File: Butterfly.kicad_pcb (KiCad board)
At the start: 2 copper layers, 93.1 x 65.5 mm, 0 parts

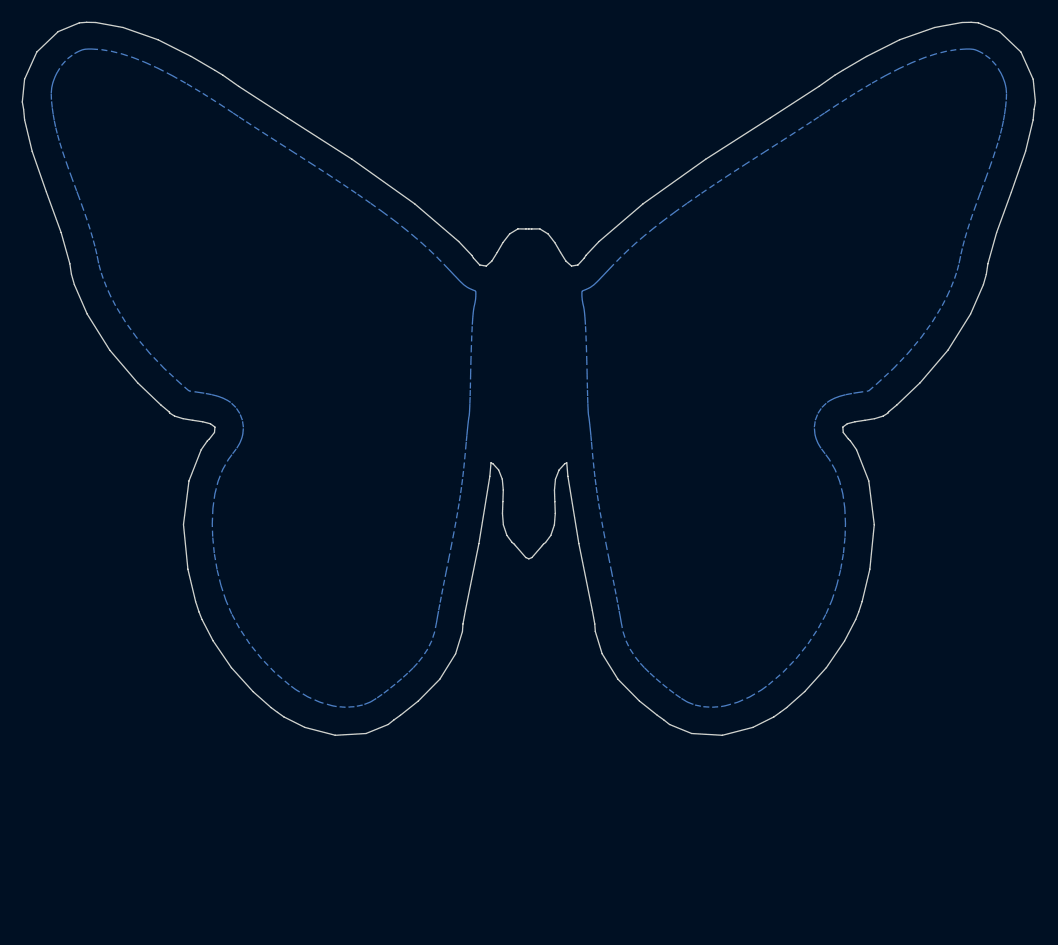
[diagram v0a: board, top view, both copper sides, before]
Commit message: Change copper layer to F.Cu.
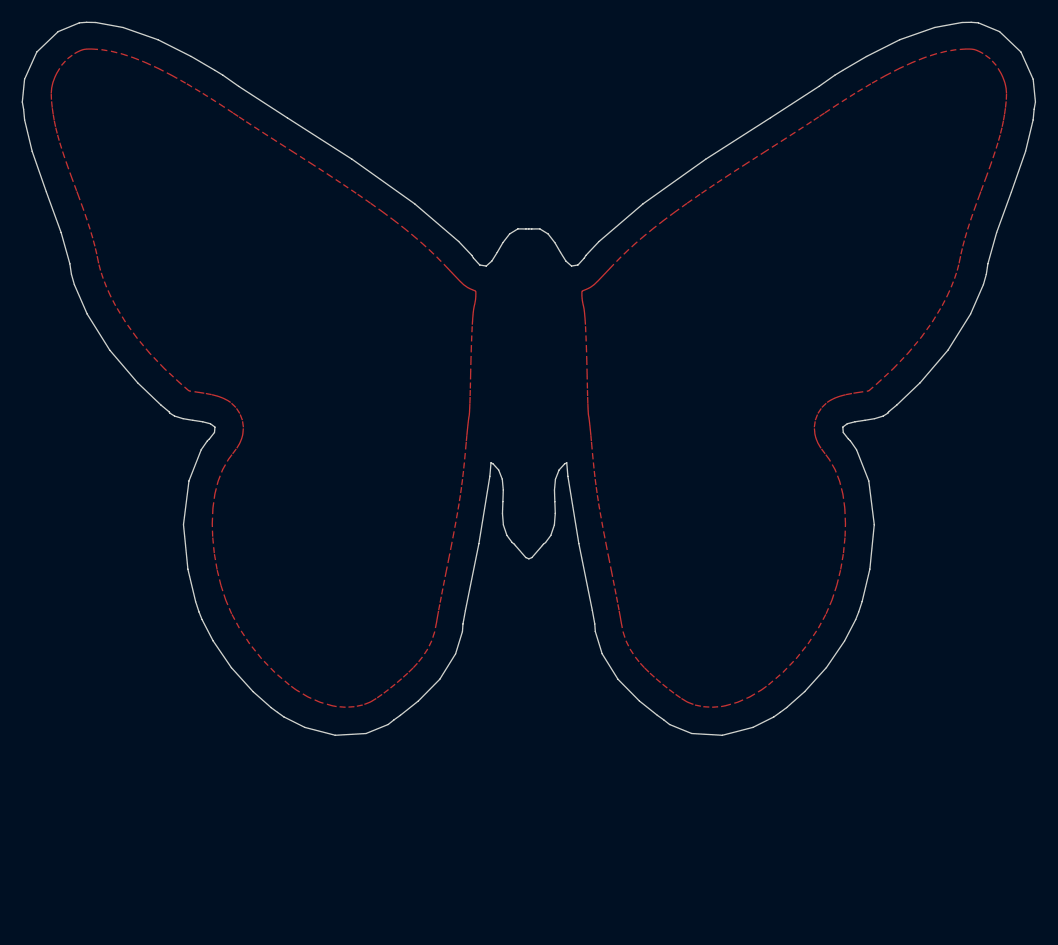
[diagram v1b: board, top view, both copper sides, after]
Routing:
- added copper zone on F.Cu, net (none)
- removed copper zone on B.Cu, net (none)
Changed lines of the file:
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@@
   (gr_line (start 161.23777 81.9574) (end 167.20467 78.1404) (layer Edge.Cuts) (width 0.1))
   (gr_line (start 183.5 99.5) (end 180.94377 102.4917) (layer Edge.Cuts) (width 0.1))
-  (zone (net 0) (net_name "") (layer B.Cu) (hatch edge 0.508)
+  (zone (net 0) (net_name "") (layer F.Cu) (hatch edge 0.508)
     (connect_pads (clearance 0.508))
     (min_thickness 0.254)
@@
     )
   )
-  (zone (net 0) (net_name "") (layer B.Cu) (hatch edge 0.508)
+  (zone (net 0) (net_name "") (layer F.Cu) (hatch edge 0.508)
     (connect_pads (clearance 0.508))
     (min_thickness 0.254)

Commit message: Instantiate left wing markings.
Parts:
- added G***: LOGO, myLibrary:copper-on-wing-left, F.Cu at (121.5, 101.5)

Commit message: Copper patterns on both wings.
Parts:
- added G***: LOGO, myLibrary:copper-on-wing-right, F.Cu at (168.5, 101.5)

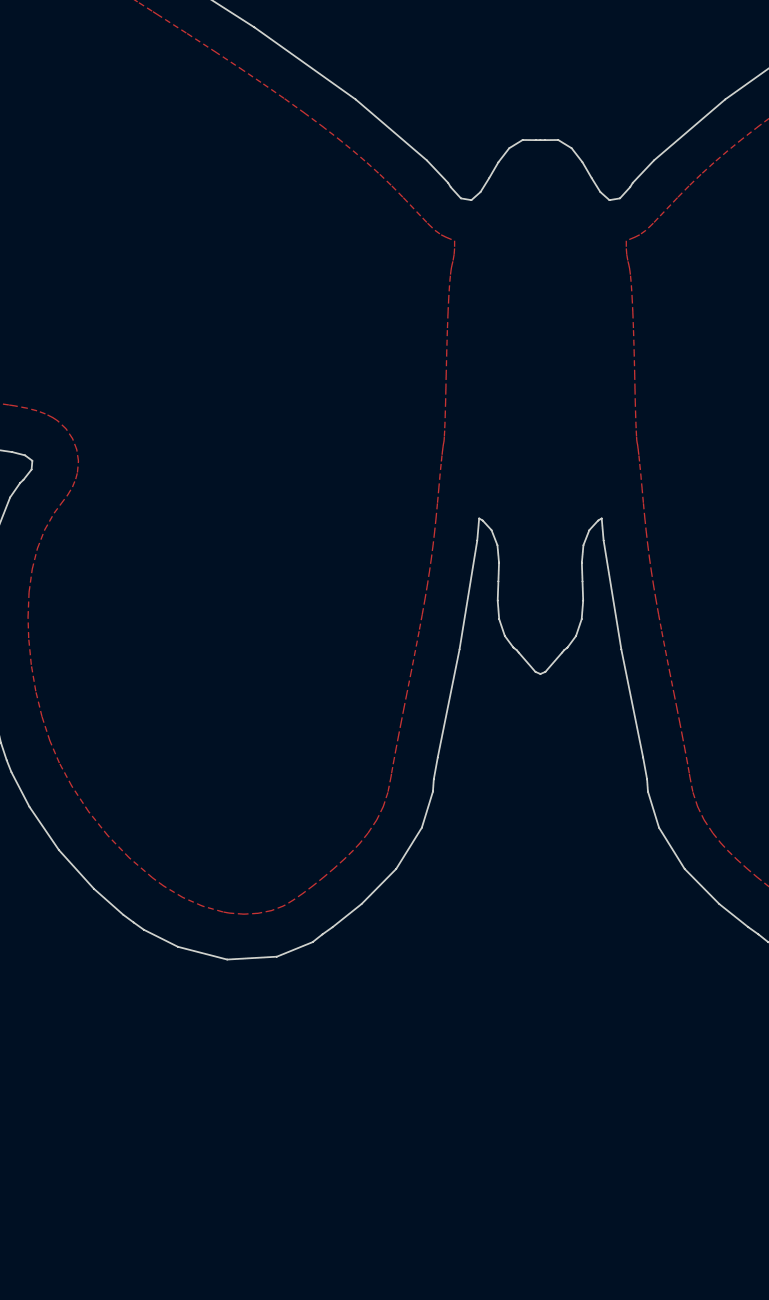
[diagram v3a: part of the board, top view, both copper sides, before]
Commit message: Trying to position footprints; not enough room.
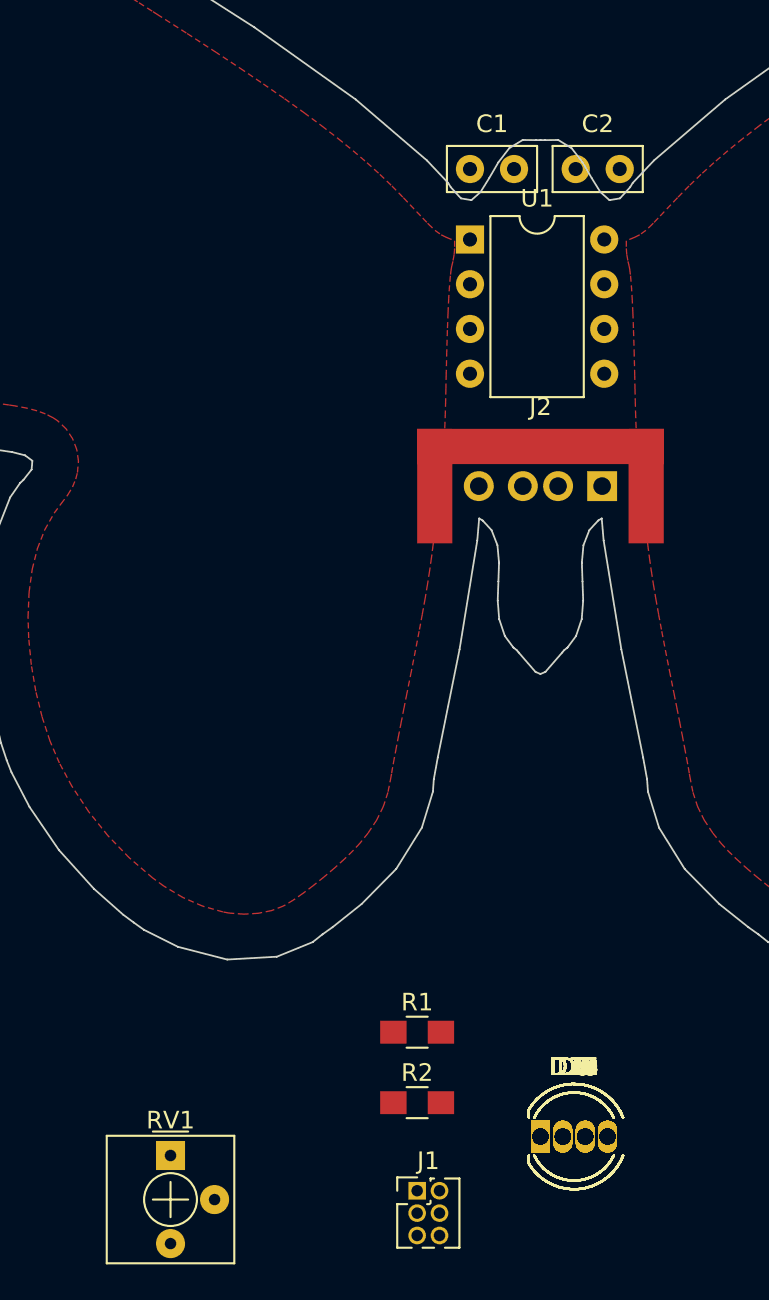
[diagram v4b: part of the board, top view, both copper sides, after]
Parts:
- added C1: 4.7uF, Capacitors_THT:C_Disc_D5.0mm_W2.5mm_P2.50mm, F.Cu at (141.0, 90.0)
- added C2: 4.7uF, Capacitors_THT:C_Disc_D5.0mm_W2.5mm_P2.50mm, F.Cu at (147.0, 90.0)
- added D1, D10, D11, D12, D13, D14, D15, D16, D17, D18, D19, D2, D20, D21, D22, D23, D24, D3, D4, D5, D6, D7, D8, D9: Neopixel_THT, LEDs:LED_D5.0mm-4, F.Cu at (145.0, 144.9)
- added J1: Conn_02x03_Odd_Even, Pin_Headers:Pin_Header_Straight_2x03_Pitch1.27mm, F.Cu at (138.0, 148.0)
- added J2: USB_A, myLibrary:USB_A_Molex-0480370001_Vertical, F.Cu at (145.0, 108.0)
- added R1: 470, Resistors_SMD:R_0805_HandSoldering, F.Cu at (138.0, 139.0)
- added R2: 10k, Resistors_SMD:R_0805_HandSoldering, F.Cu at (138.0, 143.0)
- added RV1: 10k, Potentiometers:Potentiometer_Trimmer_Copal_CT-6EP, F.Cu at (124.0, 146.0)
- added U1: ATTINY85-20PU, Housings_DIP:DIP-8_W7.62mm, F.Cu at (141.0, 94.0)

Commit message: Moving stuff around.
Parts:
- moved J1 35.7 mm to (145.0, 113.0)
- moved U1 9.00 mm to (141.0, 103.0), turned to 90 degrees
- moved C1 2.00 mm to (141.0, 92.0), turned to 45 degrees
- turned C2 to 315 degrees
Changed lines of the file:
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@@
   )
   (module Capacitors_THT:C_Disc_D5.0mm_W2.5mm_P2.50mm (layer F.Cu)
-    (at 141 90)
+    (at 141 92 45)
     (descr "C, Disc series, Radial, pin pitch=2.50mm, , diameter*width=5*2.5mm^2, Capacitor, http://cdn-reichelt.de/documents/datenblatt/B300/DS_KERKO_TC.pdf")
     (tags "C Disc series Radial pin pitch 2.50mm  diameter 5mm width 2.5mm Capacitor")
-    (fp_text reference C1 (at 1.25 -2.56) (layer F.SilkS)
-      (effects (font (size 1 1) (thickness 0.15)))
-    )
-    (fp_text value 4.7uF (at 1.25 2.56) (layer F.Fab)
+    (fp_text reference C1 (at 1.25 -2.56 45) (layer F.SilkS)
+      (effects (font (size 1 1) (thickness 0.15)))
+    )
+    (fp_text value 4.7uF (at 1.25 2.56 45) (layer F.Fab)
       (effects (font (size 1 1) (thickness 0.15)))
     )
@@
     (fp_line (start 4.1 1.6) (end 4.1 -1.6) (layer F.CrtYd) (width 0.05))
     (fp_line (start 4.1 -1.6) (end -1.6 -1.6) (layer F.CrtYd) (width 0.05))
-    (fp_text user %R (at 1.25 0) (layer F.Fab)
-      (effects (font (size 1 1) (thickness 0.15)))
-    )
-    (pad 1 thru_hole circle (at 0 0) (size 1.6 1.6) (drill 0.8) (layers *.Cu *.Mask)
-      (net 1 +5V))
-    (pad 2 thru_hole circle (at 2.5 0) (size 1.6 1.6) (drill 0.8) (layers *.Cu *.Mask)
+    (fp_text user %R (at 1.25 0 45) (layer F.Fab)
+      (effects (font (size 1 1) (thickness 0.15)))
+    )
+    (pad 1 thru_hole circle (at 0 0 45) (size 1.6 1.6) (drill 0.8) (layers *.Cu *.Mask)
+      (net 1 +5V))
+    (pad 2 thru_hole circle (at 2.5 0 45) (size 1.6 1.6) (drill 0.8) (layers *.Cu *.Mask)
       (net 2 GND))
     (model ${KISYS3DMOD}/Capacitors_THT.3dshapes/C_Disc_D5.0mm_W2.5mm_P2.50mm.wrl
@@
   )
   (module Capacitors_THT:C_Disc_D5.0mm_W2.5mm_P2.50mm (layer F.Cu)
-    (at 147 90)
+    (at 147 90 315)
     (descr "C, Disc series, Radial, pin pitch=2.50mm, , diameter*width=5*2.5mm^2, Capacitor, http://cdn-reichelt.de/documents/datenblatt/B300/DS_KERKO_TC.pdf")
     (tags "C Disc series Radial pin pitch 2.50mm  diameter 5mm width 2.5mm Capacitor")
-    (fp_text reference C2 (at 1.25 -2.56) (layer F.SilkS)
-      (effects (font (size 1 1) (thickness 0.15)))
-    )
-    (fp_text value 4.7uF (at 1.25 2.56) (layer F.Fab)
+    (fp_text reference C2 (at 1.25 -2.56 315) (layer F.SilkS)
+      (effects (font (size 1 1) (thickness 0.15)))
+    )
+    (fp_text value 4.7uF (at 1.25 2.56 315) (layer F.Fab)
       (effects (font (size 1 1) (thickness 0.15)))
     )
@@
     (fp_line (start 4.1 1.6) (end 4.1 -1.6) (layer F.CrtYd) (width 0.05))
     (fp_line (start 4.1 -1.6) (end -1.6 -1.6) (layer F.CrtYd) (width 0.05))
-    (fp_text user %R (at 1.25 0) (layer F.Fab)
-      (effects (font (size 1 1) (thickness 0.15)))
-    )
-    (pad 1 thru_hole circle (at 0 0) (size 1.6 1.6) (drill 0.8) (layers *.Cu *.Mask)
-      (net 1 +5V))
-    (pad 2 thru_hole circle (at 2.5 0) (size 1.6 1.6) (drill 0.8) (layers *.Cu *.Mask)
+    (fp_text user %R (at 1.25 0 315) (layer F.Fab)
+      (effects (font (size 1 1) (thickness 0.15)))
+    )
+    (pad 1 thru_hole circle (at 0 0 315) (size 1.6 1.6) (drill 0.8) (layers *.Cu *.Mask)
+      (net 1 +5V))
+    (pad 2 thru_hole circle (at 2.5 0 315) (size 1.6 1.6) (drill 0.8) (layers *.Cu *.Mask)
       (net 2 GND))
     (model ${KISYS3DMOD}/Capacitors_THT.3dshapes/C_Disc_D5.0mm_W2.5mm_P2.50mm.wrl
@@
   )
   (module Pin_Headers:Pin_Header_Straight_2x03_Pitch1.27mm (layer F.Cu)
-    (at 138 148)
+    (at 145 113)
     (descr "Through hole straight pin header, 2x03, 1.27mm pitch, double rows")
     (tags "Through hole pin header THT 2x03 1.27mm double row")
@@
   )
   (module Housings_DIP:DIP-8_W7.62mm (layer F.Cu)
-    (at 141 94)
+    (at 141 103 90)
     (descr "8-lead though-hole mounted DIP package, row spacing 7.62 mm (300 mils)")
     (tags "THT DIP DIL PDIP 2.54mm 7.62mm 300mil")
-    (fp_text reference U1 (at 3.81 -2.33) (layer F.SilkS)
-      (effects (font (size 1 1) (thickness 0.15)))
-    )
-    (fp_text value ATTINY85-20PU (at 3.81 9.95) (layer F.Fab)
+    (fp_text reference U1 (at 3.81 -2.33 90) (layer F.SilkS)
+      (effects (font (size 1 1) (thickness 0.15)))
+    )
+    (fp_text value ATTINY85-20PU (at 3.81 9.95 90) (layer F.Fab)
       (effects (font (size 1 1) (thickness 0.15)))
     )
@@
     (fp_line (start 8.7 9.15) (end 8.7 -1.55) (layer F.CrtYd) (width 0.05))
     (fp_line (start 8.7 -1.55) (end -1.1 -1.55) (layer F.CrtYd) (width 0.05))
-    (fp_text user %R (at 3.81 3.81) (layer F.Fab)
-      (effects (font (size 1 1) (thickness 0.15)))
-    )
-    (pad 1 thru_hole rect (at 0 0) (size 1.6 1.6) (drill 0.8) (layers *.Cu *.Mask)
+    (fp_text user %R (at 3.81 3.81 90) (layer F.Fab)
+      (effects (font (size 1 1) (thickness 0.15)))
+    )
+    (pad 1 thru_hole rect (at 0 0 90) (size 1.6 1.6) (drill 0.8) (layers *.Cu *.Mask)
       (net 31 "Net-(J1-Pad5)"))
-    (pad 5 thru_hole oval (at 7.62 7.62) (size 1.6 1.6) (drill 0.8) (layers *.Cu *.Mask)
+    (pad 5 thru_hole oval (at 7.62 7.62 90) (size 1.6 1.6) (drill 0.8) (layers *.Cu *.Mask)
       (net 30 "Net-(J1-Pad4)"))
-    (pad 2 thru_hole oval (at 0 2.54) (size 1.6 1.6) (drill 0.8) (layers *.Cu *.Mask)
+    (pad 2 thru_hole oval (at 0 2.54 90) (size 1.6 1.6) (drill 0.8) (layers *.Cu *.Mask)
       (net 34 "Net-(R1-Pad2)"))
-    (pad 6 thru_hole oval (at 7.62 5.08) (size 1.6 1.6) (drill 0.8) (layers *.Cu *.Mask)
+    (pad 6 thru_hole oval (at 7.62 5.08 90) (size 1.6 1.6) (drill 0.8) (layers *.Cu *.Mask)
       (net 28 "Net-(J1-Pad1)"))
-    (pad 3 thru_hole oval (at 0 5.08) (size 1.6 1.6) (drill 0.8) (layers *.Cu *.Mask)
+    (pad 3 thru_hole oval (at 0 5.08 90) (size 1.6 1.6) (drill 0.8) (layers *.Cu *.Mask)
       (net 35 "Net-(RV1-Pad2)"))
-    (pad 7 thru_hole oval (at 7.62 2.54) (size 1.6 1.6) (drill 0.8) (layers *.Cu *.Mask)
+    (pad 7 thru_hole oval (at 7.62 2.54 90) (size 1.6 1.6) (drill 0.8) (layers *.Cu *.Mask)
       (net 29 "Net-(J1-Pad3)"))
-    (pad 4 thru_hole oval (at 0 7.62) (size 1.6 1.6) (drill 0.8) (layers *.Cu *.Mask)
-      (net 2 GND))
-    (pad 8 thru_hole oval (at 7.62 0) (size 1.6 1.6) (drill 0.8) (layers *.Cu *.Mask)
+    (pad 4 thru_hole oval (at 0 7.62 90) (size 1.6 1.6) (drill 0.8) (layers *.Cu *.Mask)
+      (net 2 GND))
+    (pad 8 thru_hole oval (at 7.62 0 90) (size 1.6 1.6) (drill 0.8) (layers *.Cu *.Mask)
       (net 1 +5V))
     (model ${KISYS3DMOD}/Housings_DIP.3dshapes/DIP-8_W7.62mm.wrl
